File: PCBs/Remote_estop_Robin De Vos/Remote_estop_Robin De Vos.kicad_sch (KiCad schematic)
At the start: 22 parts, among them J1 UART connector, SW1 SW_Push, SW2 SW_Push, SW3 SW_Push, U1 ESP32-WROOM-32E, U2 AMS1117-3.3

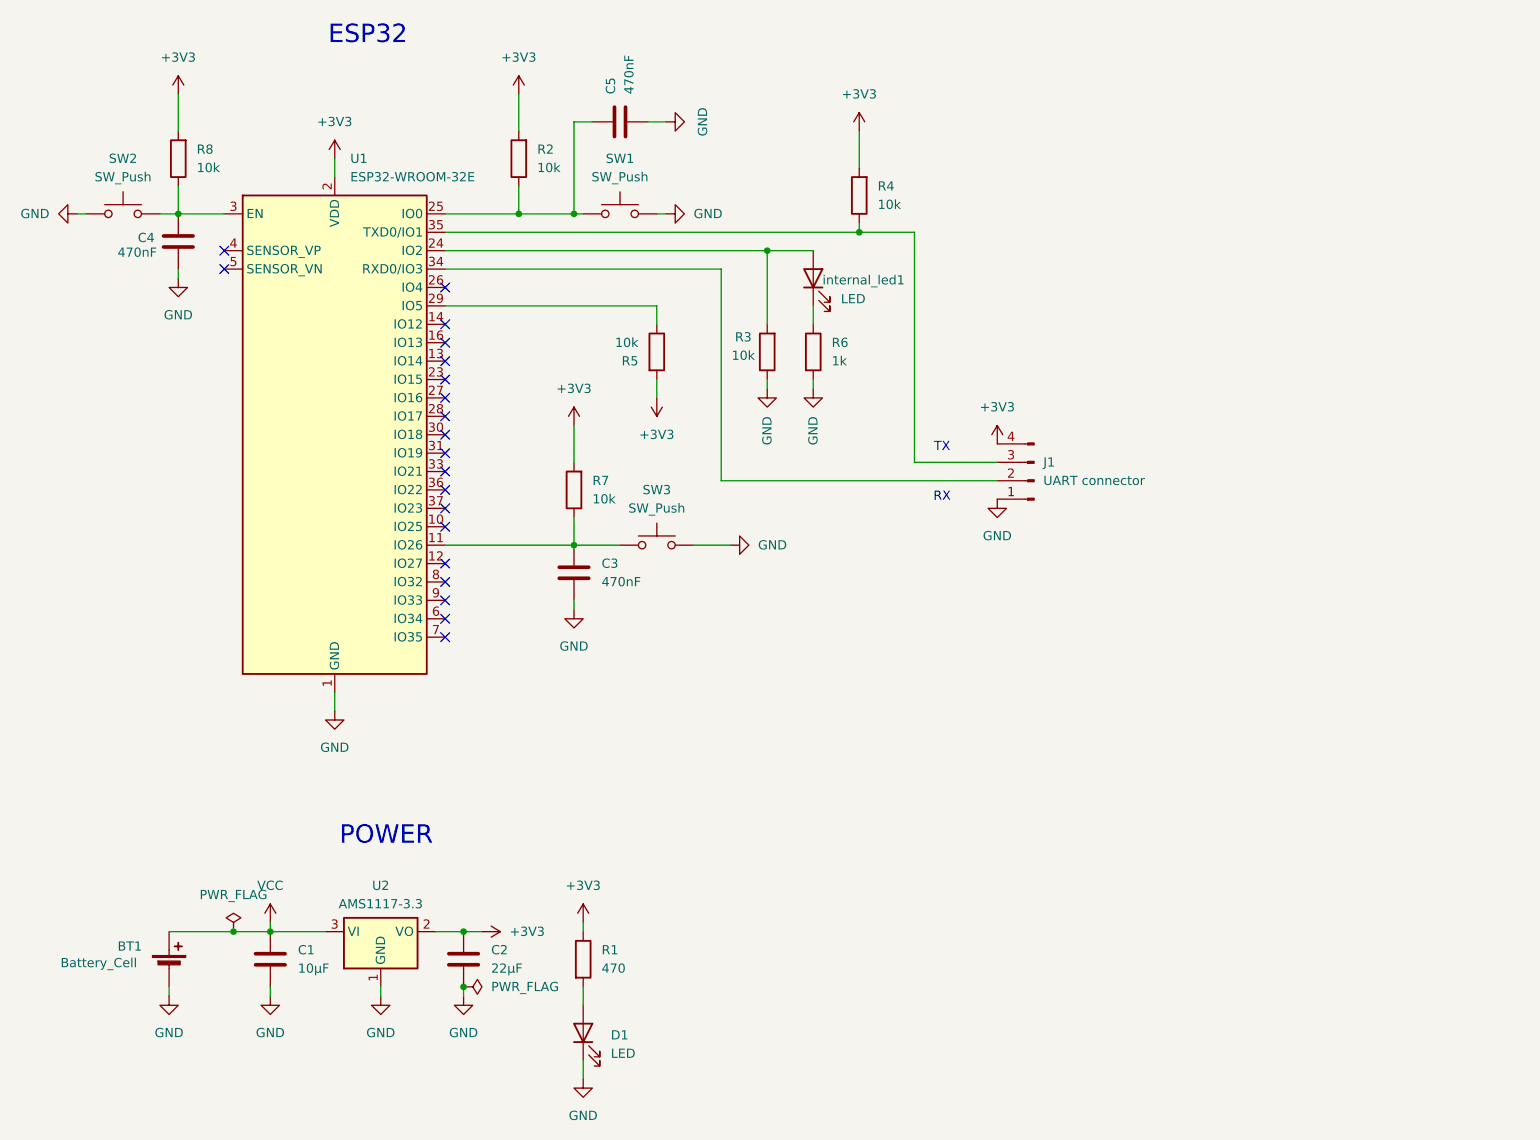
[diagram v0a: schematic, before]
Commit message: pcb remote estop v1
eerste versie van pcb met slechte routing
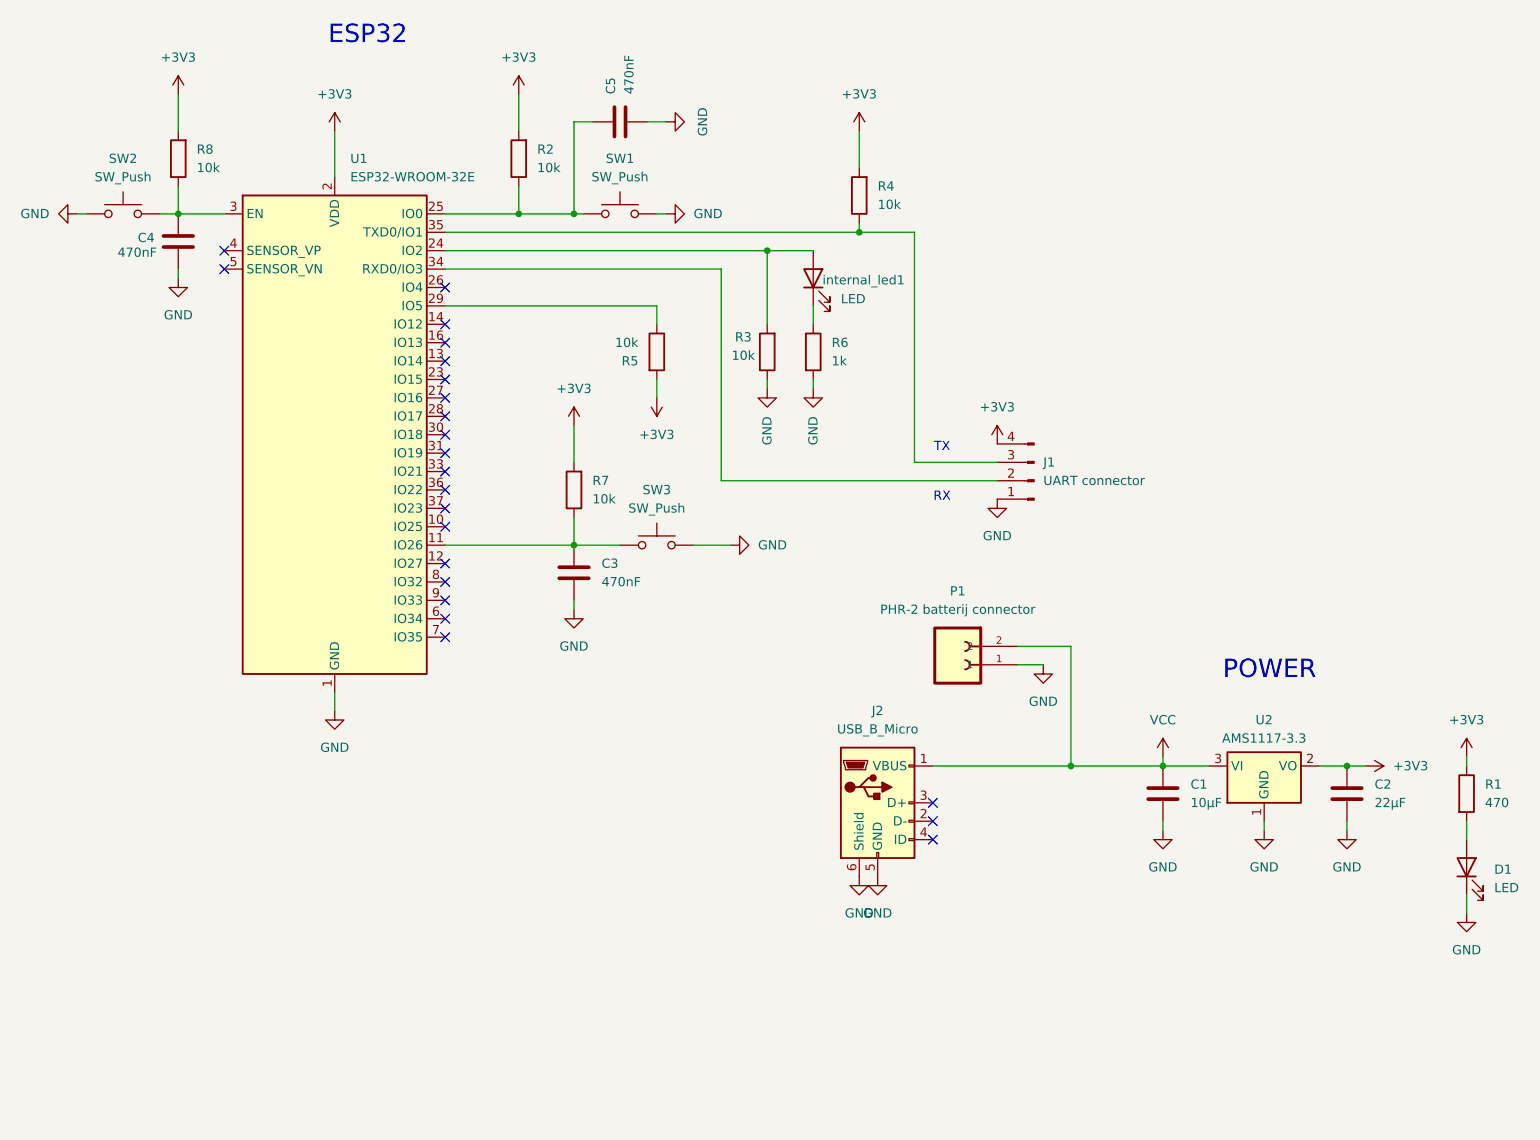
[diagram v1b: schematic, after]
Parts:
- removed BT1: Battery_Cell, symbol Device:Battery_Cell
- added J2: USB_B_Micro, Connector_USB:USB_Micro-B_Molex-105017-0001, symbol Connector:USB_B_Micro
- added P1: PHR-2 batterij connector, PHR-2:JST_PHR-2, symbol PHR-2:PHR-2
- C1, C2, C3, C4, C5: footprint (none) -> Capacitor_SMD:C_0805_2012Metric_Pad1.18x1.45mm_HandSolder
- D1, internal_led1: footprint (none) -> LED_SMD:LED_0805_2012Metric_Pad1.15x1.40mm_HandSolder
- J1: footprint (none) -> Connector_PinHeader_2.54mm:PinHeader_1x04_P2.54mm_Vertical
- R1, R2, R3, R4, R5, R6, R7, R8: footprint (none) -> Resistor_SMD:R_0805_2012Metric_Pad1.20x1.40mm_HandSolder
- SW1, SW2, SW3: footprint (none) -> Button_Switch_SMD:434111043826
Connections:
- net GND: now also J2.5 (GND), J2.6 (Shield), P1.1
- net VCC: now also J2.1 (VBUS), P1.2
- no-connect marks 20 -> 23
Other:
- moved on the sheet: C1, C2, D1, R1, U2

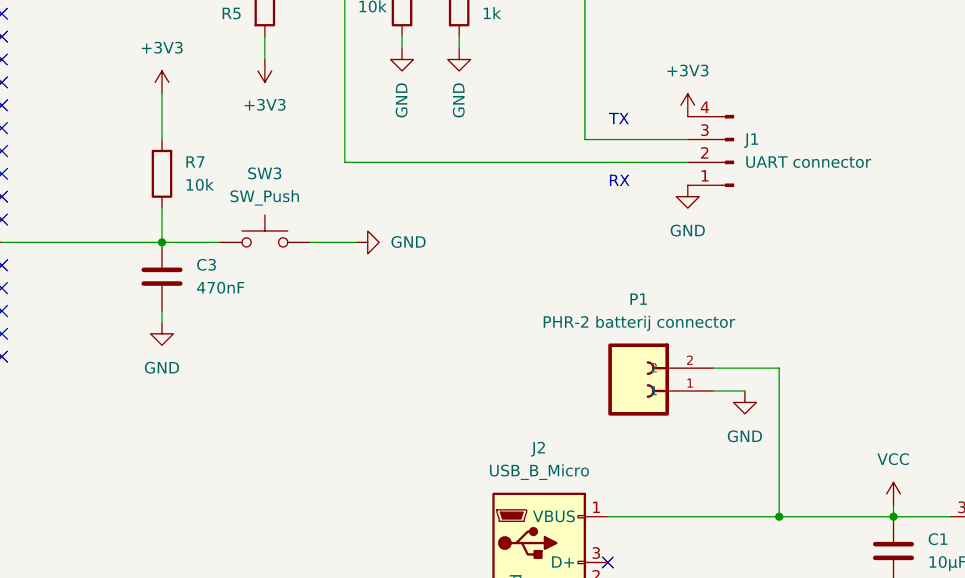
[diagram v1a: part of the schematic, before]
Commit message: pcb remote estop v2
Versie 2 met betere routing en begin van de silkscreen
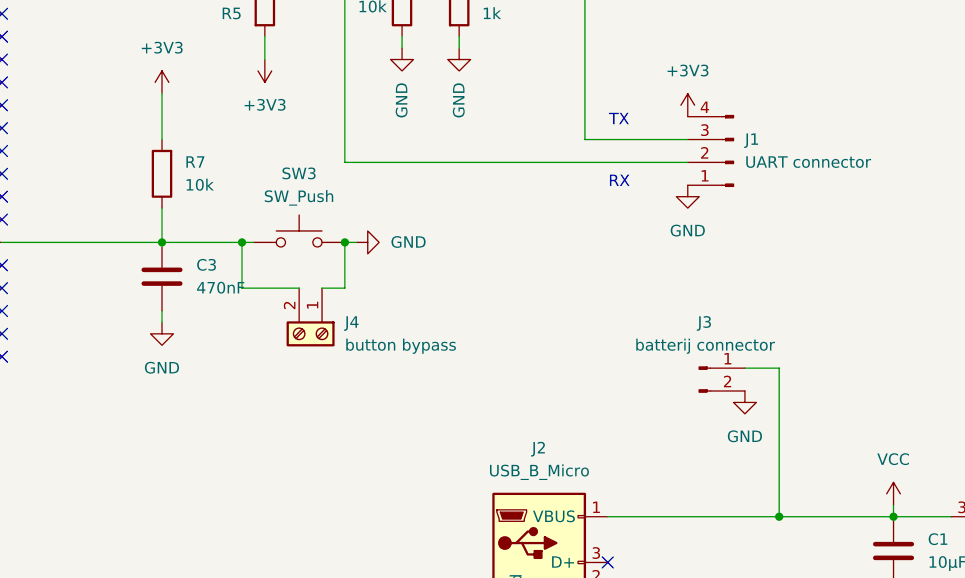
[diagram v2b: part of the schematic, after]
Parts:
- removed P1: PHR-2 batterij connector, PHR-2:JST_PHR-2, symbol PHR-2:PHR-2
- added J3: batterij connector, Connector_PinHeader_2.54mm:PinHeader_1x02_P2.54mm_Vertical, symbol Connector:Conn_01x02_Pin
- added J4: button bypass, TerminalBlock:TerminalBlock_MaiXu_MX126-5.0-02P_1x02_P5.00mm, symbol Connector:Screw_Terminal_01x02
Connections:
- net GND: now also J3.2 (Pin_2), J4.1 (Pin_1)
- net VCC: now also J3.1 (Pin_1)
- net at C3.1, R7.1, SW3.1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: now also J4.2 (Pin_2)
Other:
- moved on the sheet: SW3
